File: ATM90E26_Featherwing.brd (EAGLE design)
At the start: 49.9 x 39.4 mm, 56 parts, among them J1 ST-PJ-312, J2 4P-SMD-2.0-90D, J3 4P-SMD-2.0-90D, J4 12V AC, Q1 8.192MHz, U1 ATM90E26, U2 CJT1117-5.0-SOT223

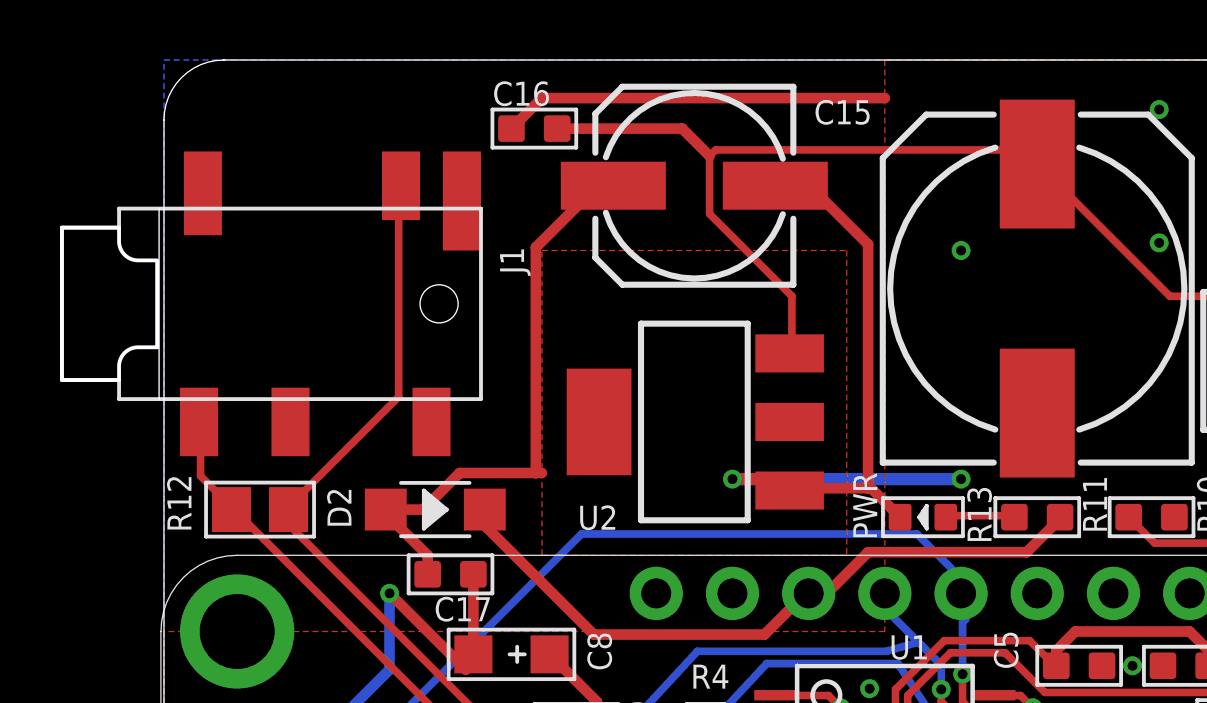
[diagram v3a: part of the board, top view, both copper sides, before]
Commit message: 1 left over airwire
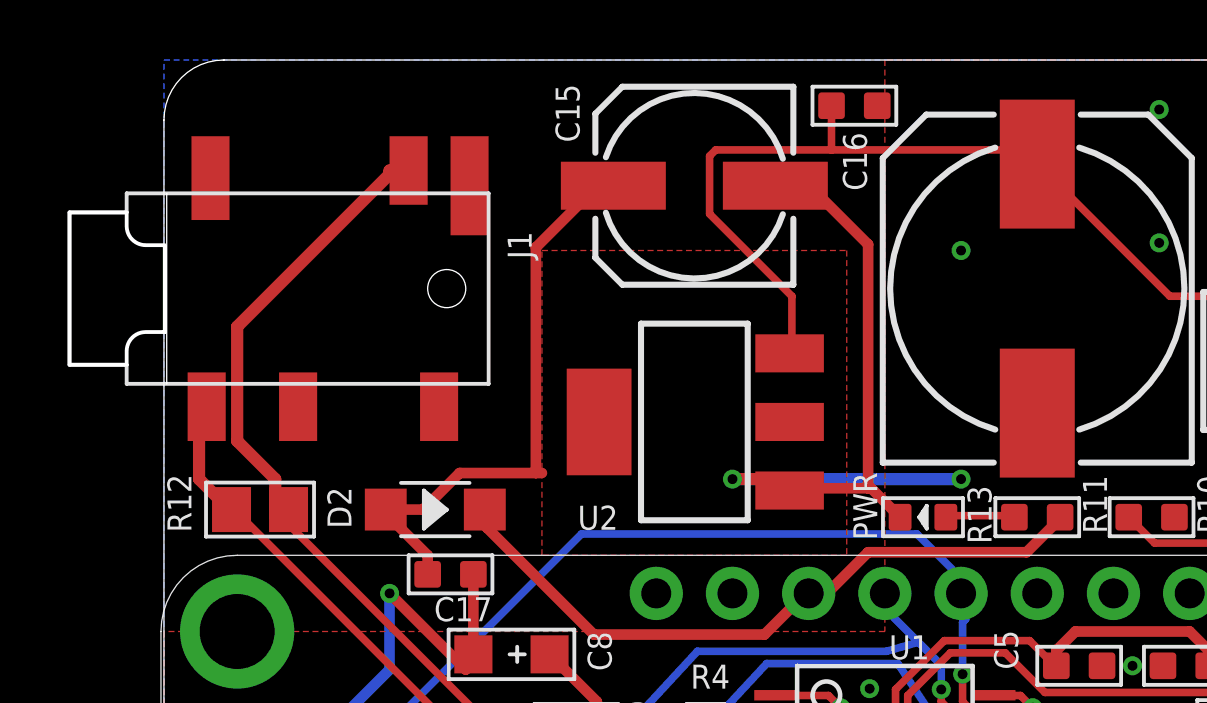
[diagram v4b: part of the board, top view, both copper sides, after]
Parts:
- moved C16 10.7 mm to (23.1, 37.8), turned to 180 degrees
- moved J1 0.57 mm to (-3.05, 31.8)
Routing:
- net GND: track 60.0 -> 46.8 mm
- net N$4: track 33.2 -> 29.2 mm
- net I1P_IN: track 27.8 -> 30.7 mm
- net I1N_IN: track 22.1 -> 24.6 mm
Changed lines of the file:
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@@
 <layer number="19" name="Unrouted" color="6" fill="1" visible="yes" active="yes"/>
 <layer number="20" name="Dimension" color="15" fill="1" visible="yes" active="yes"/>
-<layer number="21" name="tPlace" color="7" fill="1" visible="no" active="yes"/>
-<layer number="22" name="bPlace" color="13" fill="1" visible="no" active="yes"/>
+<layer number="21" name="tPlace" color="7" fill="1" visible="yes" active="yes"/>
+<layer number="22" name="bPlace" color="13" fill="1" visible="yes" active="yes"/>
 <layer number="23" name="tOrigins" color="15" fill="1" visible="yes" active="yes"/>
 <layer number="24" name="bOrigins" color="15" fill="1" visible="yes" active="yes"/>
-<layer number="25" name="tNames" color="7" fill="1" visible="no" active="yes"/>
-<layer number="26" name="bNames" color="13" fill="1" visible="no" active="yes"/>
+<layer number="25" name="tNames" color="7" fill="1" visible="yes" active="yes"/>
+<layer number="26" name="bNames" color="13" fill="1" visible="yes" active="yes"/>
 <layer number="27" name="tValues" color="7" fill="1" visible="no" active="yes"/>
 <layer number="28" name="bValues" color="7" fill="1" visible="no" active="yes"/>
@@
 </element>
 <element name="C15" library="adafruit" package="153CLV-0605" value="100uF" x="17.78" y="35.179" smashed="yes" rot="R180">
-<attribute name="NAME" x="23.71" y="38.026" size="0.8" layer="25" font="vector" ratio="20" rot="R180"/>
+<attribute name="NAME" x="13.155" y="38.569" size="0.8" layer="25" font="vector" ratio="20" rot="R270"/>
 <attribute name="VALUE" x="21.205" y="40.064" size="0.8" layer="27" rot="R180"/>
 </element>
@@
 <attribute name="VALUE" x="27.305" y="25.8445" size="0.8" layer="27" ratio="11" rot="R180"/>
 </element>
-<element name="J1" library="Seeed-OPL-Connector" package="AUDIO6P-SMD-3.5-14.0X6.4X5.0MM" value="ST-PJ-312" x="-3.302" y="31.242" smashed="yes" rot="R180">
-<attribute name="NAME" x="11.303" y="33.147" size="0.8" layer="25" font="vector" ratio="20" rot="R270"/>
-<attribute name="VALUE" x="6.858" y="35.687" size="0.8" layer="27" ratio="11" rot="R180"/>
+<element name="J1" library="Seeed-OPL-Connector" package="AUDIO6P-SMD-3.5-14.0X6.4X5.0MM" value="ST-PJ-312" x="-3.048" y="31.75" smashed="yes" rot="R180">
+<attribute name="NAME" x="11.557" y="33.655" size="0.8" layer="25" font="vector" ratio="20" rot="R270"/>
+<attribute name="VALUE" x="7.112" y="36.195" size="0.8" layer="27" ratio="11" rot="R180"/>
 </element>
 <element name="R12" library="microbuilder" package="0805" value="12R" x="3.302" y="24.384" smashed="yes">
@@
 <attribute name="NAME" x="5.474" y="9.106" size="0.8" layer="26" font="vector" ratio="20" rot="MR180"/>
 </element>
-<element name="C16" library="Discrete" package="C0603" value="100n" x="12.446" y="37.084" smashed="yes">
-<attribute name="NAME" x="11.049" y="37.846" size="0.8" layer="25" font="vector" ratio="20"/>
-<attribute name="VALUE" x="11.176" y="36.8935" size="0.8" layer="27" ratio="12"/>
-<attribute name="NAME" x="11.176" y="36.83" size="0.635" layer="33" ratio="10"/>
+<element name="C16" library="Discrete" package="C0603" value="100n" x="23.114" y="37.846" smashed="yes" rot="R180">
+<attribute name="NAME" x="22.733" y="36.957" size="0.8" layer="25" font="vector" ratio="20" rot="R270"/>
+<attribute name="VALUE" x="24.384" y="38.0365" size="0.8" layer="27" ratio="12" rot="R180"/>
+<attribute name="NAME" x="24.384" y="38.1" size="0.635" layer="33" ratio="10" rot="R180"/>
 </element>
 <element name="C17" library="Discrete" package="C0603" value="100n" x="9.652" y="22.225" smashed="yes" rot="R180">
@@
 <contactref element="C17" pad="1"/>
 <wire x1="10.414" y1="22.225" x2="10.414" y2="19.558" width="0.3556" layer="1"/>
-<wire x1="12.7" y1="38.1" x2="24.13" y2="38.1" width="0.3556" layer="1"/>
-<wire x1="11.684" y1="37.084" x2="12.7" y2="38.1" width="0.3556" layer="1"/>
-<wire x1="11.43" y1="36.83" x2="11.684" y2="37.084" width="0.3556" layer="1"/>
 <wire x1="26.67" y1="25.4" x2="19.05" y2="25.4" width="0.4064" layer="16"/>
 <wire x1="20.32" y1="25.4" x2="19.05" y2="25.4" width="0.4064" layer="1"/>
@@
 <wire x1="4.2672" y1="24.384" x2="4.2672" y2="23.876" width="0.254" layer="1"/>
 <wire x1="4.2672" y1="24.384" x2="4.252" y2="24.384" width="0.254" layer="1"/>
-<wire x1="7.9248" y1="28.1432" x2="7.9248" y2="35.1536" width="0.254" layer="1"/>
-<wire x1="4.2672" y1="24.4856" x2="7.9248" y2="28.1432" width="0.254" layer="1"/>
-<wire x1="7.9248" y1="35.1536" x2="8.001" y2="35.179" width="0.254" layer="1"/>
-<wire x1="4.2672" y1="24.4856" x2="4.252" y2="24.384" width="0.254" layer="1"/>
+<wire x1="2.54" y1="30.48" x2="7.62" y2="35.56" width="0.4064" layer="1"/>
+<wire x1="2.54" y1="26.67" x2="2.54" y2="30.48" width="0.4064" layer="1"/>
+<wire x1="3.81" y1="25.4" x2="2.54" y2="26.67" width="0.4064" layer="1"/>
+<wire x1="3.81" y1="24.13" x2="3.81" y2="25.4" width="0.4064" layer="1"/>
+<wire x1="3.81" y1="24.13" x2="4.252" y2="24.384" width="0.4064" layer="1"/>
+<wire x1="8.255" y1="35.687" x2="7.62" y2="35.687" width="0.4064" layer="1"/>
+<wire x1="7.62" y1="35.687" x2="7.62" y2="35.56" width="0.4064" layer="1"/>
 </signal>
 <signal name="I1N_IN">
@@
 <wire x1="2.4384" y1="24.384" x2="11.3792" y2="15.4432" width="0.254" layer="1"/>
 <wire x1="2.4384" y1="24.384" x2="2.352" y2="24.384" width="0.254" layer="1"/>
-<wire x1="1.3208" y1="25.5016" x2="1.3208" y2="27.2288" width="0.254" layer="1"/>
-<wire x1="2.3368" y1="24.4856" x2="1.3208" y2="25.5016" width="0.254" layer="1"/>
-<wire x1="1.3208" y1="27.2288" x2="1.27" y2="27.305" width="0.254" layer="1"/>
 <wire x1="2.3368" y1="24.4856" x2="2.352" y2="24.384" width="0.254" layer="1"/>
+<wire x1="2.3368" y1="24.5872" x2="2.7432" y2="24.9936" width="0.254" layer="1"/>
+<wire x1="2.3368" y1="24.5872" x2="2.352" y2="24.384" width="0.254" layer="1"/>
+<wire x1="1.27" y1="25.4" x2="1.27" y2="27.94" width="0.4064" layer="1"/>
+<wire x1="2.54" y1="24.13" x2="1.27" y2="25.4" width="0.4064" layer="1"/>
+<wire x1="1.27" y1="27.94" x2="1.524" y2="27.813" width="0.4064" layer="1"/>
+<wire x1="2.54" y1="24.13" x2="2.352" y2="24.384" width="0.4064" layer="1"/>
 </signal>
 <signal name="I2P_IN">
@@
 <wire x1="18.288" y1="36.1696" x2="18.288" y2="34.2392" width="0.254" layer="1"/>
 <wire x1="18.4912" y1="36.3728" x2="18.288" y2="36.1696" width="0.254" layer="1"/>
-<wire x1="28.7528" y1="36.3728" x2="18.4912" y2="36.3728" width="0.254" layer="1"/>
+<wire x1="28.7528" y1="36.3728" x2="22.352" y2="36.3728" width="0.254" layer="1"/>
+<wire x1="22.352" y1="36.3728" x2="18.4912" y2="36.3728" width="0.254" layer="1"/>
 <wire x1="29.1592" y1="35.9664" x2="28.7528" y2="36.3728" width="0.254" layer="1"/>
 <wire x1="21.0312" y1="29.6672" x2="20.955" y2="29.591" width="0.254" layer="1"/>
 <wire x1="29.1592" y1="35.9664" x2="29.21" y2="35.9" width="0.254" layer="1"/>
 <contactref element="C16" pad="2"/>
-<wire x1="13.208" y1="37.084" x2="17.3736" y2="37.084" width="0.3556" layer="1"/>
-<wire x1="17.3736" y1="37.084" x2="18.288" y2="36.1696" width="0.3556" layer="1"/>
+<wire x1="22.352" y1="36.3728" x2="22.352" y2="37.846" width="0.254" layer="1"/>
 </signal>
 <signal name="V_OUT" class="1">
